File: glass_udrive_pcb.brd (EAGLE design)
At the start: 8.5 x 19 mm, 14 parts, among them J1 OMNETICS_A75243-001

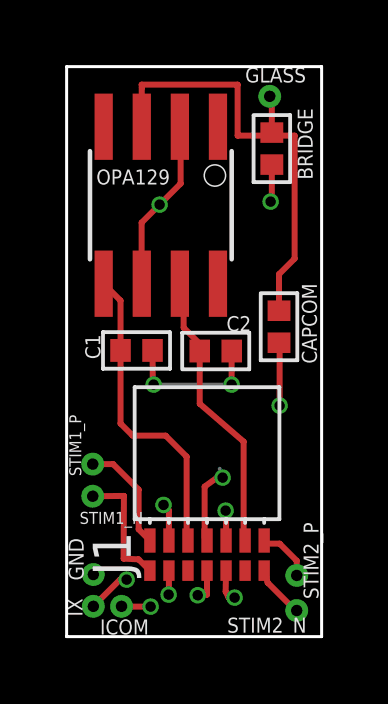
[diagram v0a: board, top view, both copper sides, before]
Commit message: Galen's suggested changes to Rev 1.0
I have changed a number of things in your design, one of which is major and the
rest are minor. The major change is that I have added a guard trace to your
design, in accordance with the data sheet for the OPA129. If you are going to
use an ultra-low input bias current op amp, then you should make efforts to
actually achieve the performance that it touts. The other changes are mostly
positioning to accommodate the guard trace, changes to the silk screen on your
board, and simplification of the routing of some traces.

To achieve very low input bias, you need to make sure that there is no leakage
current to the electrode net from the rest of the PCB. There is some parasitic
resistance between neighboring traces in the PCB through the insulator and the
solder-mask. By surrounding the electrode with a copper trace that is driven to
be the same voltage as the electrode, this eliminates parasitic resistance, and
also reduces the stray capacitance of the electrode. I am mainly just following
the recommendations of the data sheet for the OPA129, so for more details see the
data sheet. I moved the bridge resistor and compensation capacitor closer to the
electrode to minimize the length of the electrode trace on your board, since
it's a high impedance trace that should be minimized and protected to avoid
noise pickup. I also placed the cap and res so that the guard trace runs between
the pads. To be honest, with these in place the point of using the OPA129 is
lost on me, since you'll have more parasitic current through these than through
any op amp. However, if you do not place them (which you probably will not need
to), then you will have very little input bias current. Running the trace
through the pads is manufacturable at PCBWay (0.1mm minimum), but may cost more.
I think the difference in cost will be totally worth it. We're not that price
sensitive. I also added a break in the solder mask for the guard traces, once
again to minimize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
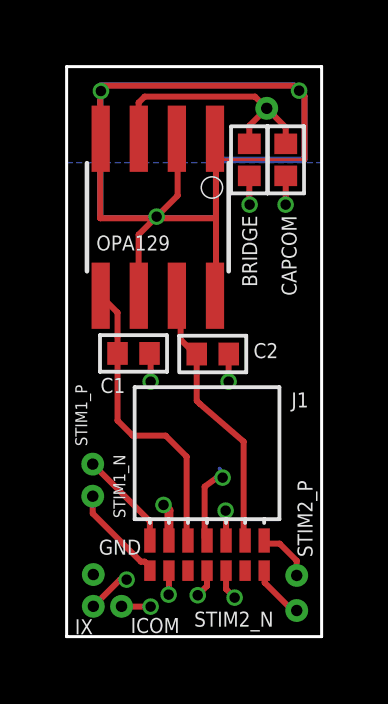
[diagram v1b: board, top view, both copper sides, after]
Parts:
- moved CAPCOM 5.57 mm to (7.30, 15.9)
- moved BRIDGE 0.84 mm to (6.09, 15.9)
- moved GLASS 0.41 mm to (6.67, 17.6)
- moved OPA129 0.41 mm to (3.04, 14.0)
- moved C1 0.14 mm to (2.23, 9.44)
- moved C2 0.14 mm to (4.87, 9.42)
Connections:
- net SIGNAL_OUT: now also OPA129.8
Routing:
- net SIGNAL_OUT: track 21.2 -> 112.0 mm, vias 2 -> 4
- net ELECTRODE: track 15.6 -> 9.29 mm
- net CAP_COM: track 11.2 -> 16.4 mm
- net GND: track 7.72 -> 4.72 mm
- net BRG_BAL: track 16.6 -> 15.4 mm
- net STIM1_N: track 4.16 -> 3.34 mm
- net I_X: track 6.29 -> 5.74 mm
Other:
- board text added: "Glass uDrive Rev 1.0"
